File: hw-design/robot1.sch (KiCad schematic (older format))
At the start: 0 parts

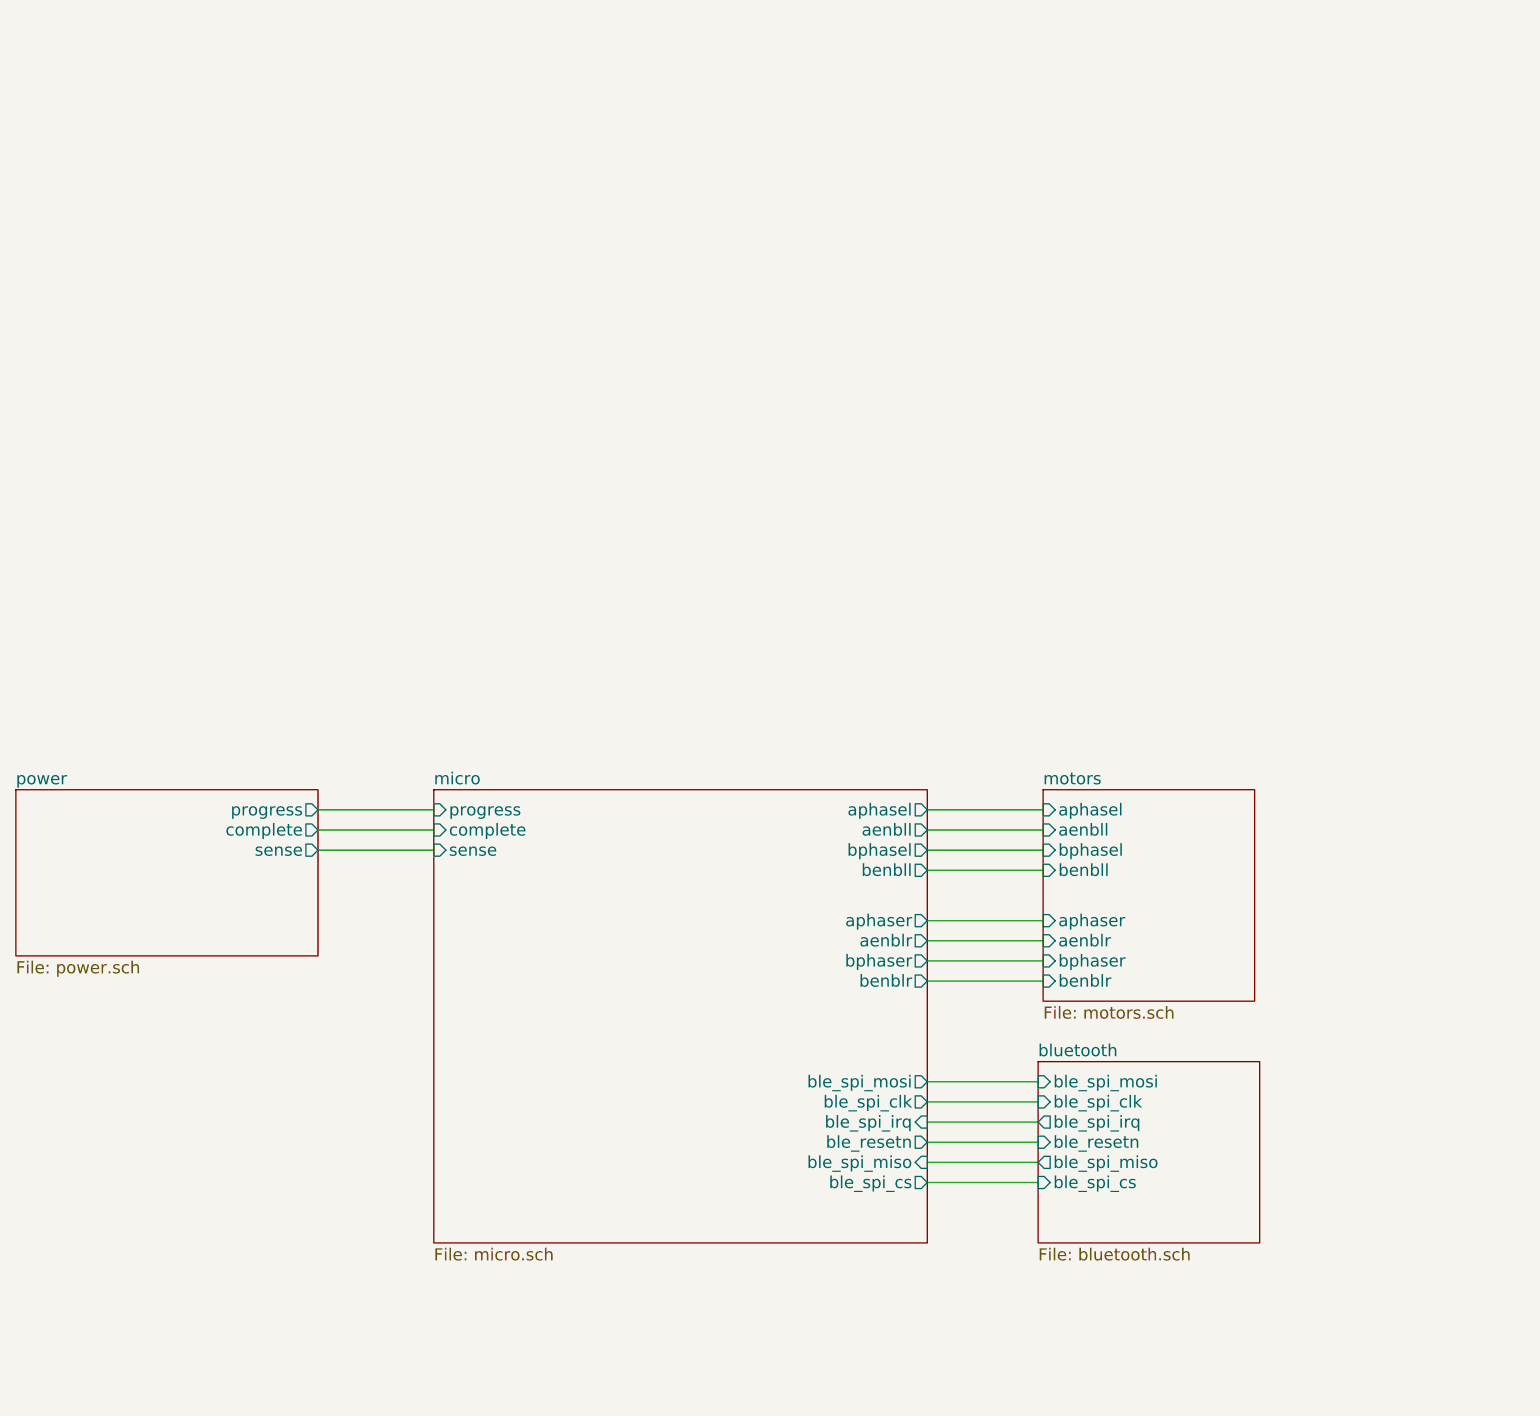
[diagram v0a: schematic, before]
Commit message: 3 boards split
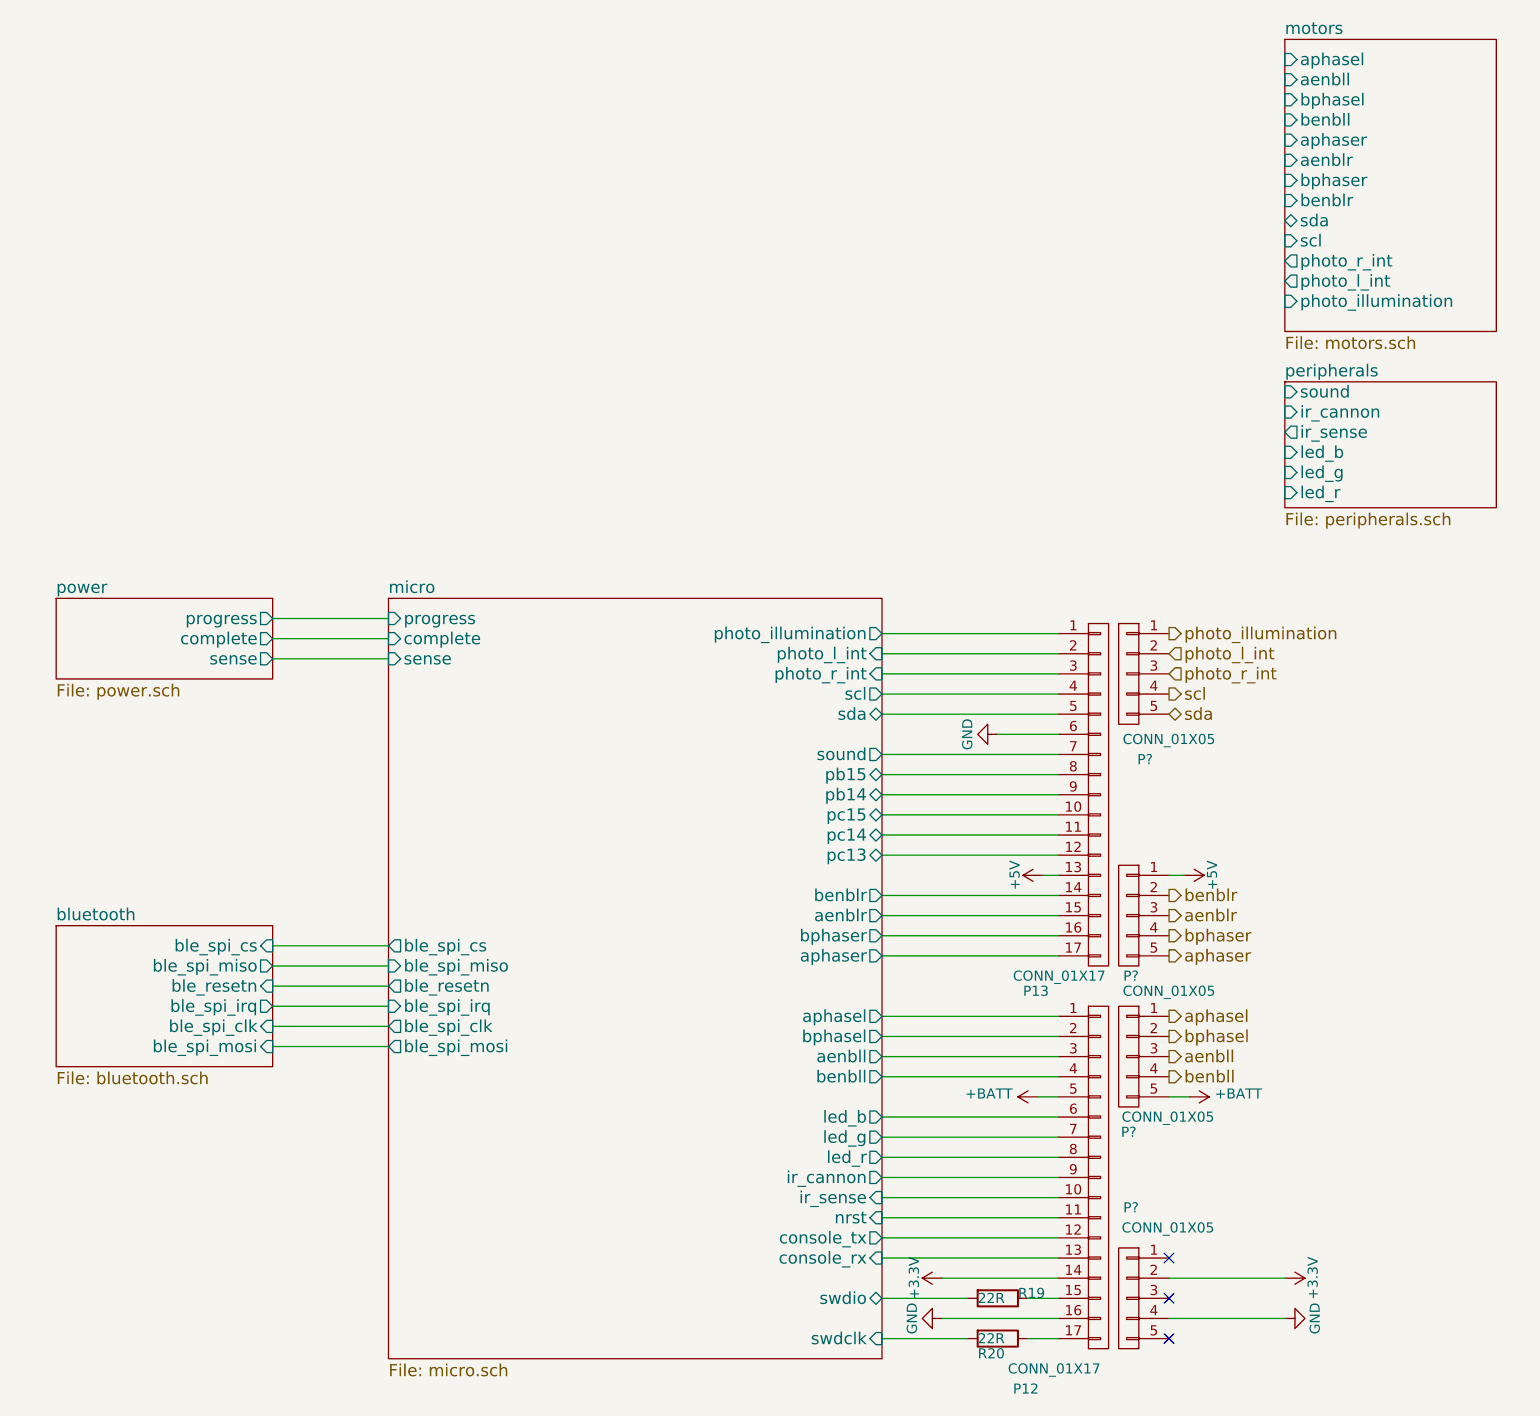
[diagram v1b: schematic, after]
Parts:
- added P12, P13: CONN_01X17, w_pin_strip:pin_strip_17, symbol CONN_01X17
- added P? (x4): CONN_01X05, w_pin_strip:pin_strip_5, symbol CONN_01X05
- added R19, R20: 22R, w_smd_resistors:r_0402, symbol R
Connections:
- net micro/aenbll: now also P12.3 (P3)
- net micro/aenblr: now also P13.15 (P15)
- net micro/aphasel: now also P12.1 (P1)
- net micro/aphaser: now also P13.17 (P17)
- net micro/benbll: now also P12.4 (P4)
- net micro/benblr: now also P13.14 (P14)
- net micro/bphasel: now also P12.2 (P2)
- net micro/bphaser: now also P13.16 (P16)
- new net: P12.15 (P15), R19.1
- new net: P12.17 (P17), R20.1
- new net +3V3: P12.14 (P14), P?.2 (P2)
- new net +5V: P13.13 (P13), P?.1 (P1)
- new net +BATT: P12.5 (P5), P?.5 (P5)
- new net GND: P12.16 (P16), P13.6 (P6), P?.4 (P4)
- new net aenbll: P?.3 (P3)
- new net aenblr: P?.3 (P3)
- new net aphasel: P?.1 (P1)
- new net aphaser: P?.5 (P5)
- new net benbll: P?.4 (P4)
- new net benblr: P?.2 (P2)
- new net bphasel: P?.2 (P2)
- new net bphaser: P?.4 (P4)
- new net micro/console_rx: P12.13 (P13)
- new net micro/console_tx: P12.12 (P12)
- new net micro/ir_cannon: P12.9 (P9)
- new net micro/ir_sense: P12.10 (P10)
- new net micro/led_b: P12.6 (P6)
- new net micro/led_g: P12.7 (P7)
- new net micro/led_r: P12.8 (P8)
- new net micro/nrst: P12.11 (P11)
- new net micro/pb14: P13.9 (P9)
- new net micro/pb15: P13.8 (P8)
- new net micro/pc13: P13.12 (P12)
- new net micro/pc14: P13.11 (P11)
- new net micro/pc15: P13.10 (P10)
- new net micro/photo_illumination: P13.1 (P1)
- new net micro/photo_l_int: P13.2 (P2)
- new net micro/photo_r_int: P13.3 (P3)
- new net micro/scl: P13.4 (P4)
- new net micro/sda: P13.5 (P5)
- new net micro/sound: P13.7 (P7)
- new net micro/swdclk: R20.2
- new net micro/swdio: R19.2
- new net photo_illumination: P?.1 (P1)
- new net photo_l_int: P?.2 (P2)
- new net photo_r_int: P?.3 (P3)
- new net scl: P?.4 (P4)
- new net sda: P?.5 (P5)
- no-connect marks 0 -> 3

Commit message: Changed to 2 boards layout. On the top one there is only : speaker, IR stuff, RGB led.
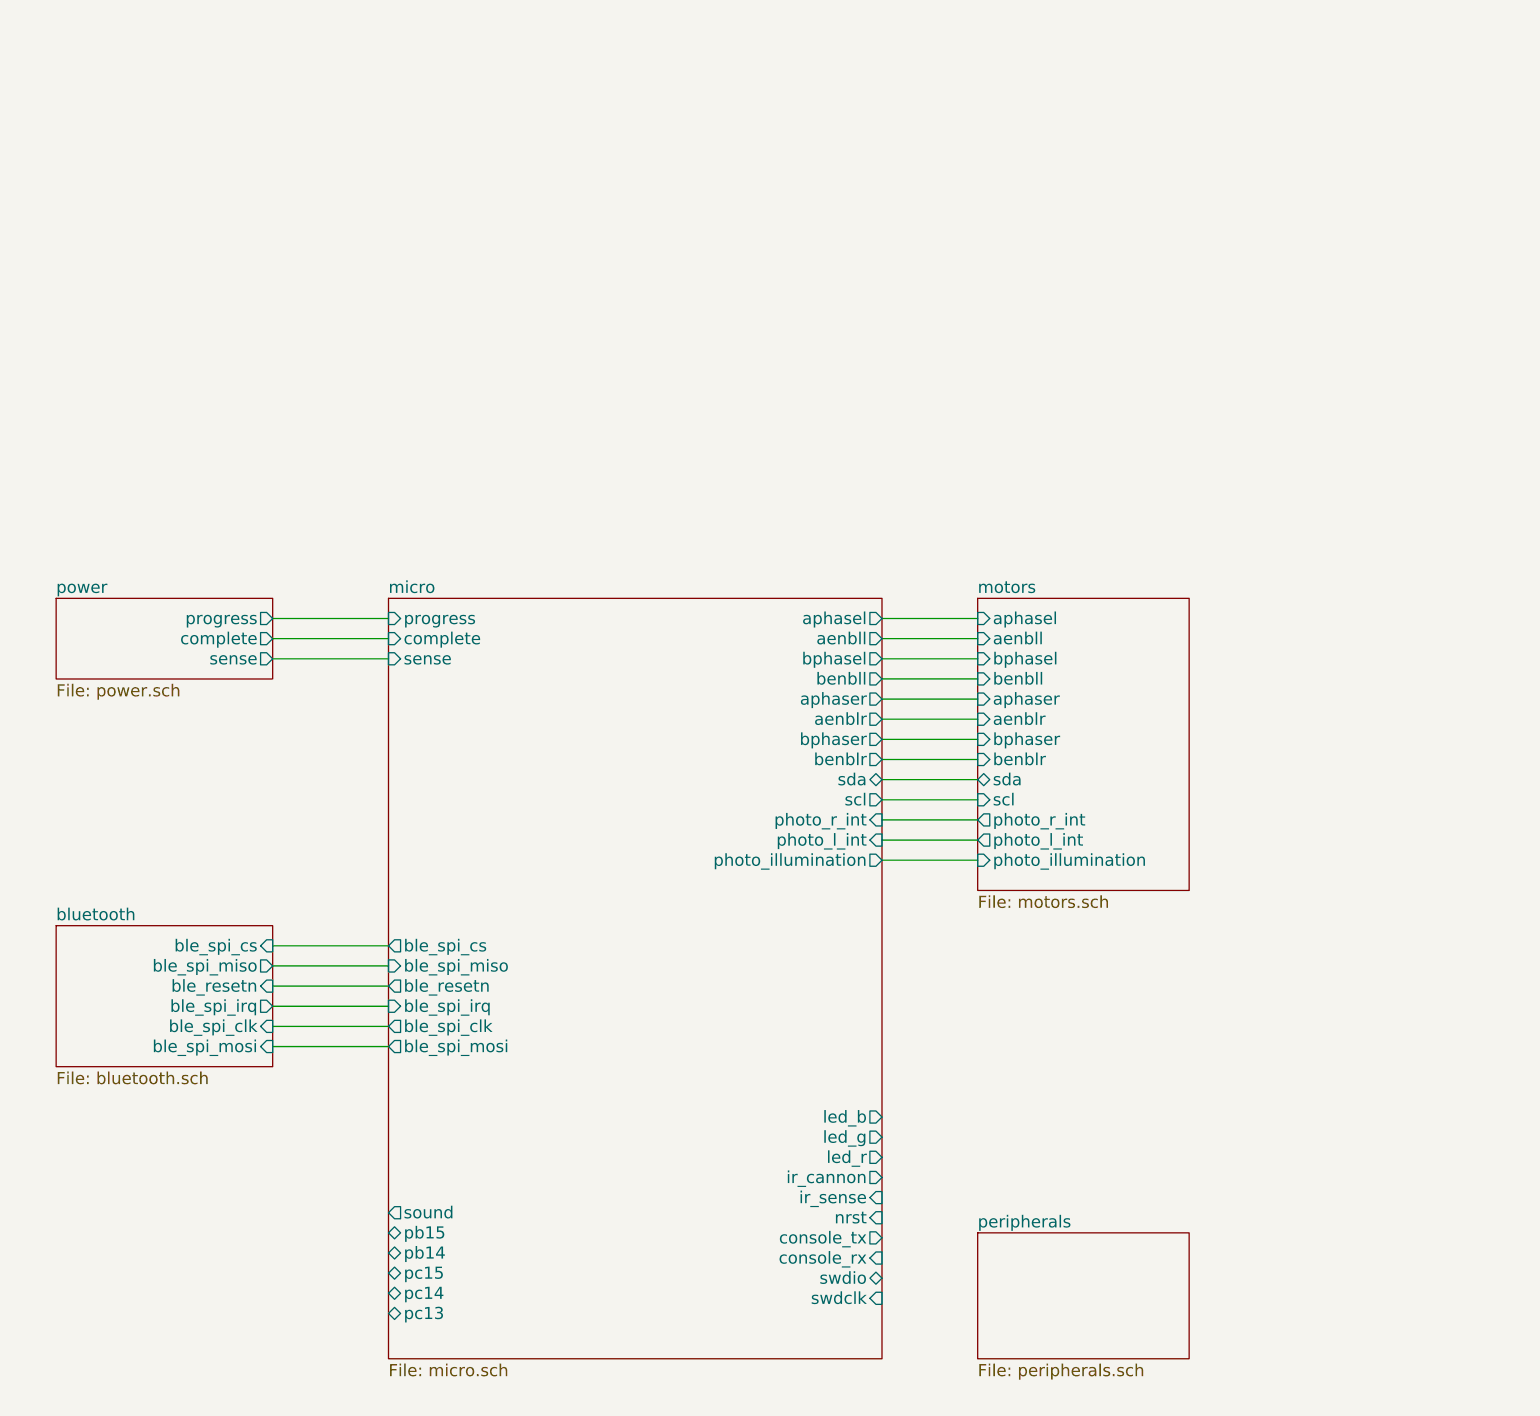
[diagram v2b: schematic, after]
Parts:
- removed P12, P13: CONN_01X17, w_pin_strip:pin_strip_17, symbol CONN_01X17
- removed P? (x4): CONN_01X05, w_pin_strip:pin_strip_5, symbol CONN_01X05
- removed R19, R20: 22R, w_smd_resistors:r_0402, symbol R
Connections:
- no-connect marks 3 -> 0

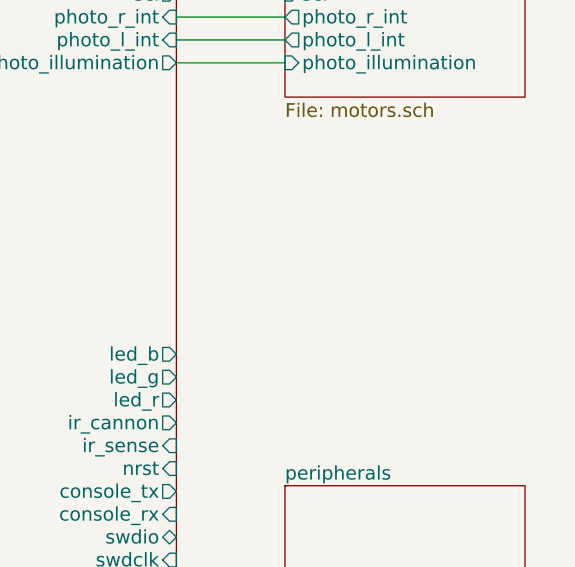
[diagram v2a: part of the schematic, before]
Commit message: Another idea of PCB split.
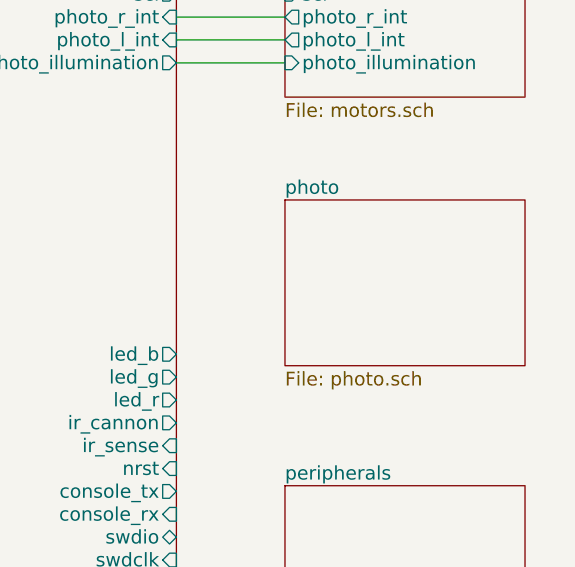
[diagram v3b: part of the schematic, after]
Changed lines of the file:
@@
 $Descr A4 11693 8268
 encoding utf-8
-Sheet 1 6
+Sheet 1 7
 Title ""
 Date ""
@@
 Wire Wire Line
 	6575 3275 7050 3275
+$Sheet
+S 7050 3875 1050 725
+U 580FC6A6
+F0 "photo" 60
+F1 "photo.sch" 60
+$EndSheet
 $EndSCHEMATC

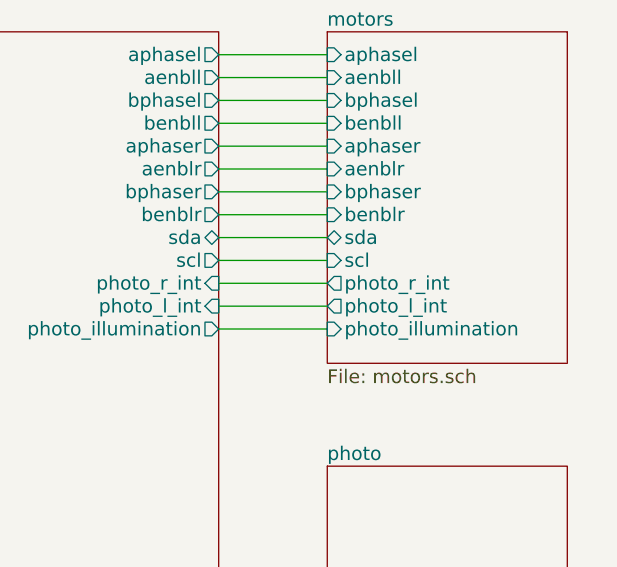
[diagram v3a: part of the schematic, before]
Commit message: 2 boards and 1 little with color sensors.
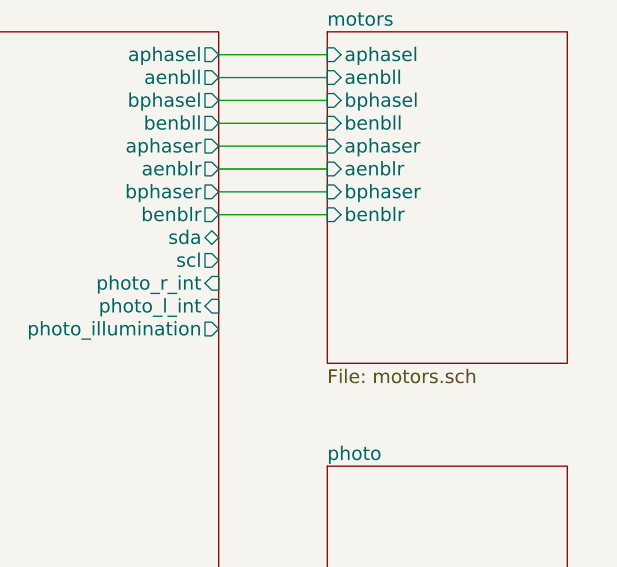
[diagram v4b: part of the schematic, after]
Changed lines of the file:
@@
 F8 "bphaser" I L 7050 2675 60
 F9 "benblr" I L 7050 2775 60
-F10 "sda" B L 7050 2875 60
-F11 "photo_l_int" O L 7050 3175 60
-F12 "scl" I L 7050 2975 60
-F13 "photo_r_int" O L 7050 3075 60
-F14 "photo_illumination" I L 7050 3275 60
 $EndSheet
 $Sheet
@@
 Wire Wire Line
 	7050 2775 6575 2775
-Wire Wire Line
-	6575 2875 7050 2875
-Wire Wire Line
-	7050 2975 6575 2975
-Wire Wire Line
-	6575 3075 7050 3075
-Wire Wire Line
-	7050 3175 6575 3175
-Wire Wire Line
-	6575 3275 7050 3275
 $Sheet
 S 7050 3875 1050 725
